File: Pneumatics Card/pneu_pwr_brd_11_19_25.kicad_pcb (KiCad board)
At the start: 4 copper layers, 59.9 x 60 mm, 62 parts, among them J1 2X1, J10 Conn_01x02, J11 Conn_01x02, J12 2X1, J2 2X1, J3 2X1, J4 2X1, J5 2X1, J6 2X1, J7 Conn_01x03_Pin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

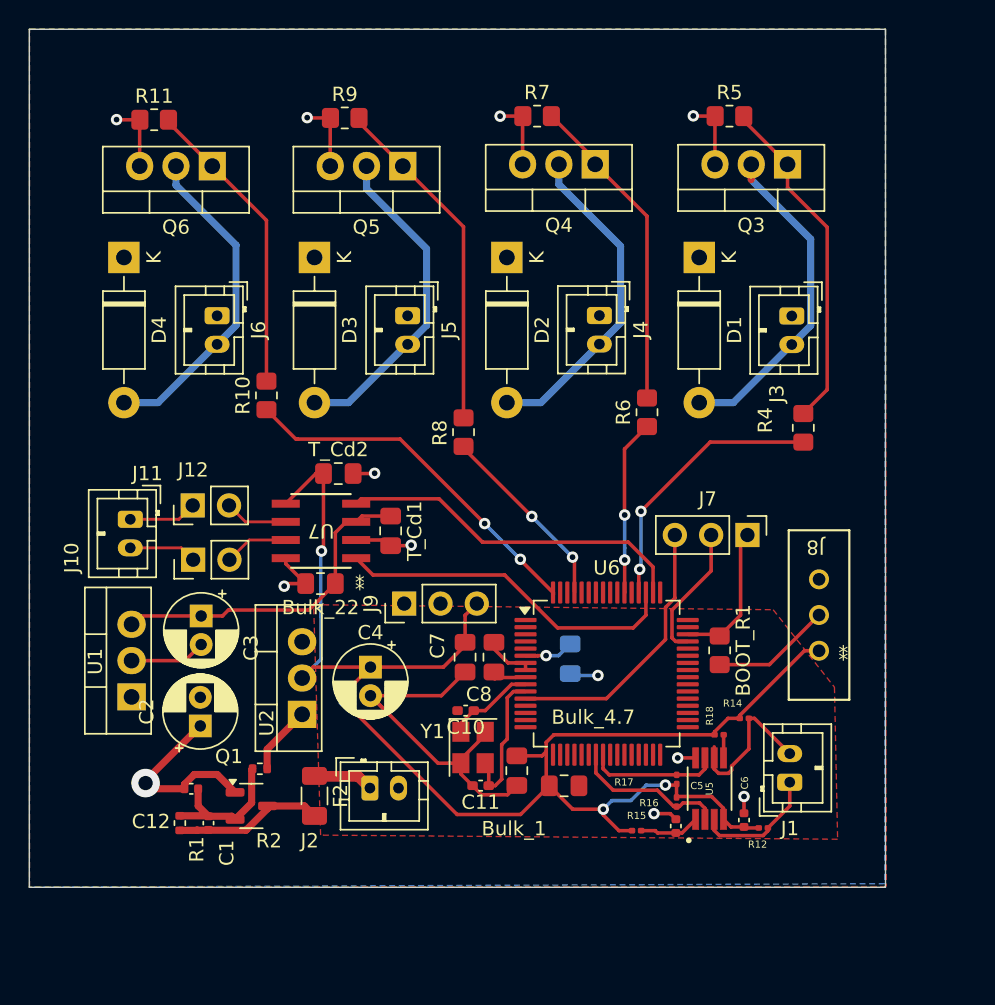
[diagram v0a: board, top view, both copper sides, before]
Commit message: Added the Mosfet drivers
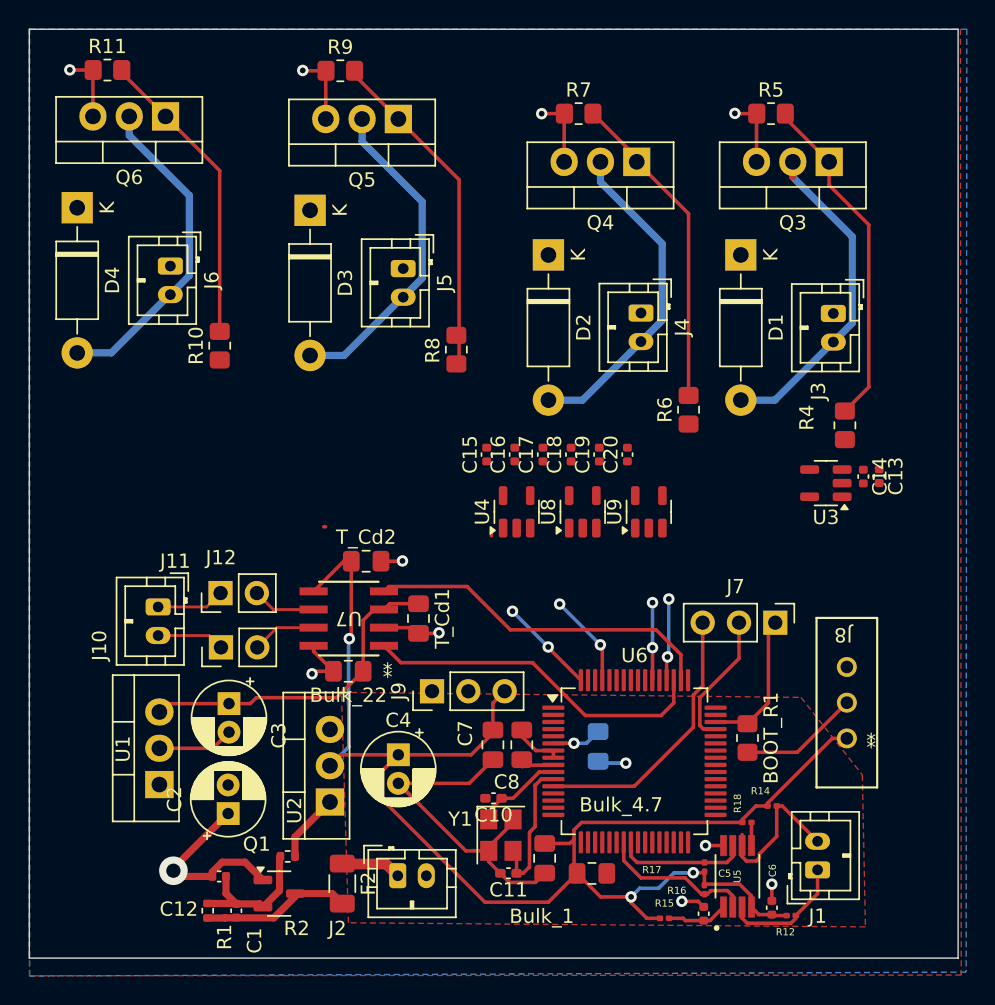
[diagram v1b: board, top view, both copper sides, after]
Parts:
- added C13: 1uF, Capacitor_SMD:C_0402_1005Metric, F.Cu at (204.8, 72.6)
- added C14: 0.1uF, Capacitor_SMD:C_0402_1005Metric, F.Cu at (203.7, 72.7)
- added C15: 0.1uF, Capacitor_SMD:C_0402_1005Metric, F.Cu at (177.3, 71.1)
- added C16: 1uF, Capacitor_SMD:C_0402_1005Metric, F.Cu at (179.3, 71.1)
- added C17: 0.1uF, Capacitor_SMD:C_0402_1005Metric, F.Cu at (181.2, 71.1)
- added C18: 1uF, Capacitor_SMD:C_0402_1005Metric, F.Cu at (183.2, 71.1)
- added C19: 0.1uF, Capacitor_SMD:C_0402_1005Metric, F.Cu at (185.2, 71.1)
- added C20: 1uF, Capacitor_SMD:C_0402_1005Metric, F.Cu at (187.1, 71.1)
- added U3: MCP1416, Package_TO_SOT_SMD:SOT-23-5, F.Cu at (201.0, 73.1)
- added U4: MCP1416, Package_TO_SOT_SMD:SOT-23-5, F.Cu at (179.4, 75.1)
- added U8: MCP1416, Package_TO_SOT_SMD:SOT-23-5, F.Cu at (184.0, 75.1)
- added U9: MCP1416, Package_TO_SOT_SMD:SOT-23-5, F.Cu at (188.6, 75.1)
- C1: value 4.7u -> 10nF
- Q1: value NTR0202PLT1G -> NTR0202PLT1G OR Si2347DS
- R1: value 47k -> 100k
- R2: value 100 -> 150k
- moved BOOT_R1 6.44 mm to (195.5, 91.0)
- moved Bulk_1 6.44 mm to (181.3, 99.4)
- moved Bulk_22 6.44 mm to (167.6, 86.3)
- moved Bulk_4.7 6.44 mm to (184.7, 100.4)
- moved C11 6.44 mm to (178.8, 100.4)
- moved C12 6.44 mm to (158.6, 100.6)
- moved C2 6.44 mm to (159.2, 96.2)
- moved C3 6.44 mm to (159.3, 88.5)
- moved C7 6.44 mm to (177.7, 91.4)
- moved C9 6.44 mm to (185.1, 91.5)
- moved F2 6.44 mm to (167.2, 101.1)
- moved J1 6.44 mm to (200.4, 100.2)
- moved J11 6.44 mm to (158.7, 80.8)
- moved J2 6.44 mm to (171.1, 100.6)
- moved J7 6.44 mm to (197.5, 82.9)
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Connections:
- R10 pad 1: S4CTRL -> Net-(U9-OUT)
- R4 pad 1: S1CTRL -> Net-(U3-OUT)
- R6 pad 1: S2CTRL -> Net-(U4-OUT)
- R8 pad 1: S3CTRL -> Net-(U8-OUT)
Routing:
- net S4CTRL: track 25.7 -> 7.24 mm
- net S1CTRL: track 19.3 -> 5.97 mm
- net S2CTRL: track 12.3 -> 5.45 mm
- net S3CTRL: track 13.4 -> 6.68 mm
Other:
- board size 59.9 x 60 mm -> 65 x 65 mm

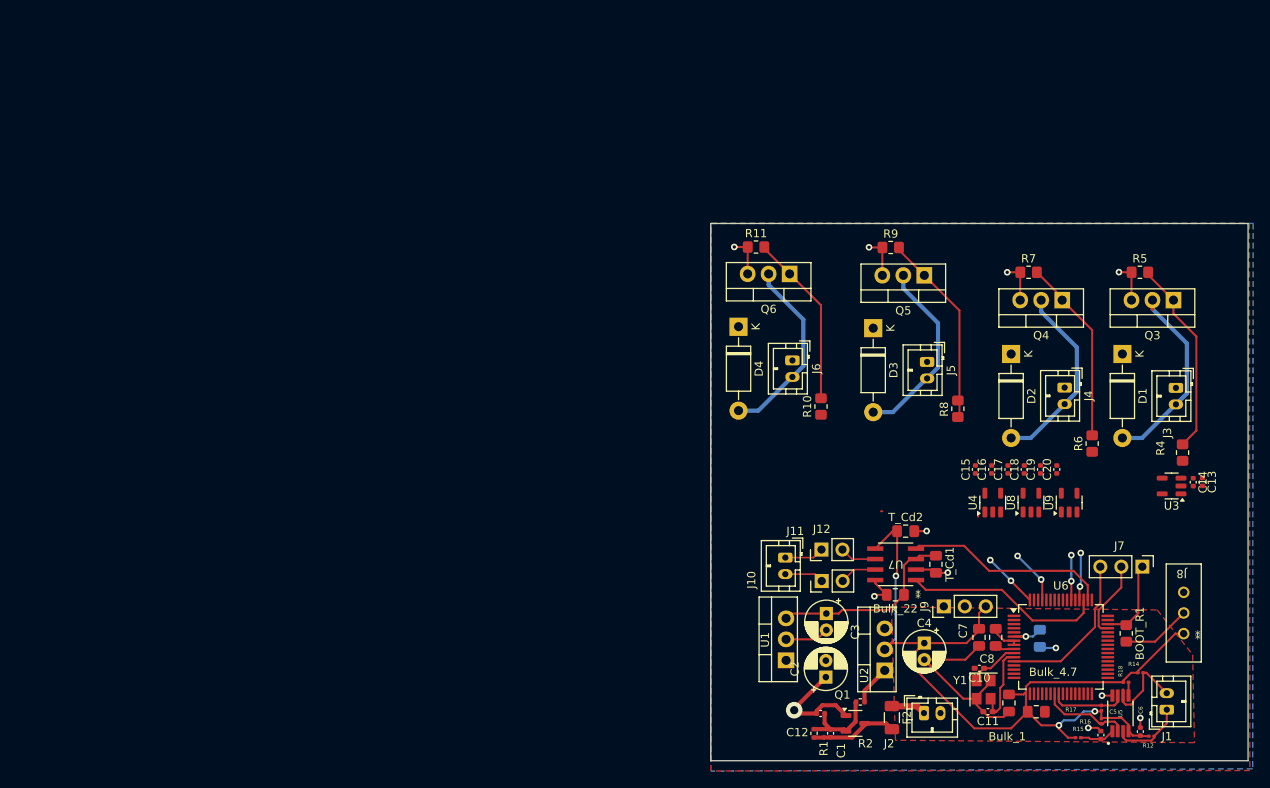
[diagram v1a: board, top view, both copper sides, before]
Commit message: Redid the Layout with new components
Increased board size to 63x63mm, added mounting holes (need to recheck), traces not routed yet.
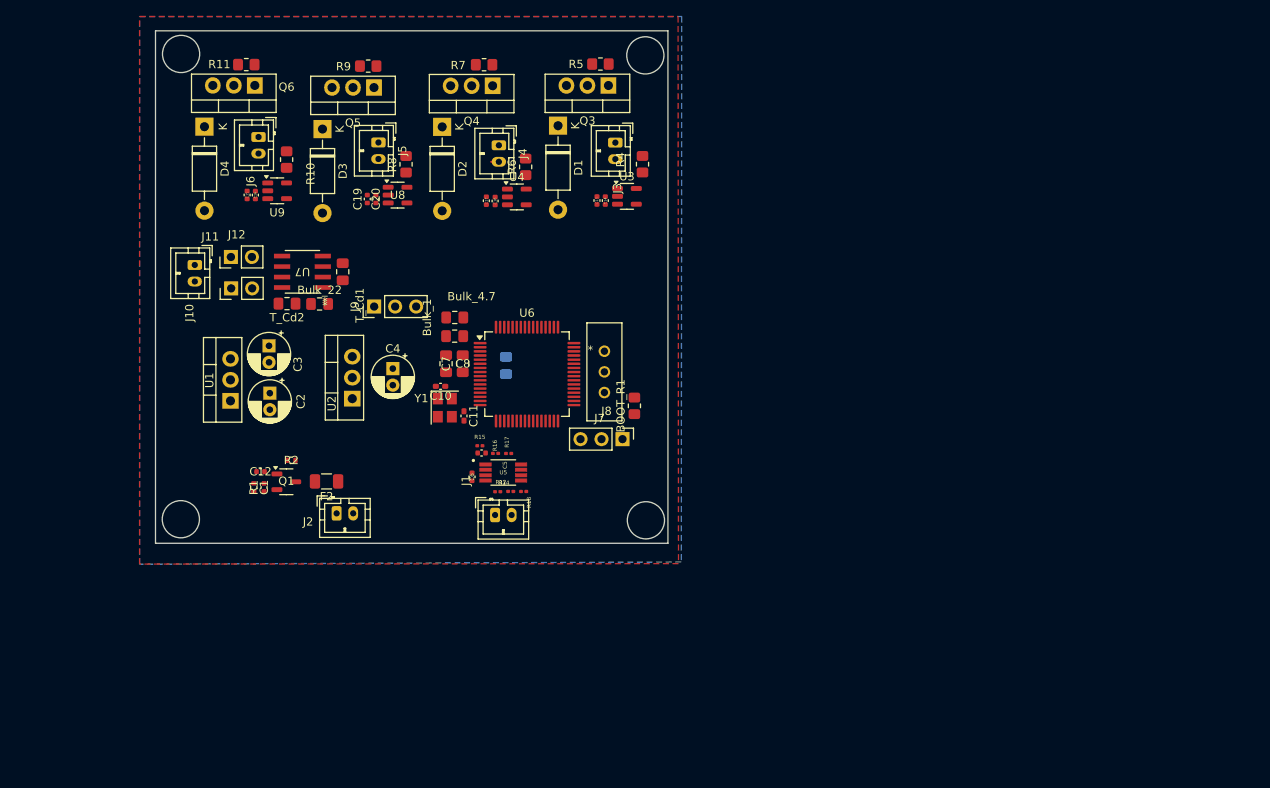
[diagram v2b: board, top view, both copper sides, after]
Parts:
- moved U9 103.0 mm to (92.8, 37.4), turned to 0 degrees
- moved C16 95.1 mm to (90.2, 37.9)
- moved C15 94.2 mm to (89.2, 37.9)
- moved C20 88.6 mm to (104.8, 38.4)
- moved C19 87.8 mm to (103.7, 38.4)
- moved C6 86.5 mm to (116.4, 72.0)
- moved U8 85.2 mm to (107.4, 37.9), turned to 0 degrees
- moved J1 84.6 mm to (119.2, 76.6), turned to 0 degrees
- moved R12 84.5 mm to (119.5, 73.8), turned to 0 degrees
- moved Bulk_4.7 83.8 mm to (114.3, 55.0)
- moved C5 82.3 mm to (117.6, 69.1), turned to 180 degrees
- moved Bulk_1 81.7 mm to (114.3, 52.7), turned to 180 degrees
- moved C13 80.8 mm to (131.5, 38.6), turned to 90 degrees
- moved R15 80.6 mm to (117.3, 68.2)
- moved U5 80.2 mm to (120.2, 71.5), turned to 0 degrees
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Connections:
- U6 pad 49: unconnected-(U6-PC9-Pad49) -> S1CTRL
- U6 pad 50: FDCAN_RX -> unconnected-(U6-PD0-Pad50)
- U6 pad 51: FDCAN_TX -> unconnected-(U6-PD1-Pad51)
- U6 pad 52: S1CTRL -> unconnected-(U6-PD2-Pad52)
- U6 pad 60: unconnected-(U6-PB6-Pad60) -> S3CTRL
- U6 pad 61: S3CTRL -> S4CTRL
- U6 pad 62: unconnected-(U6-PB8-Pad62) -> FDCAN_RX
- U6 pad 63: unconnected-(U6-PB9-Pad63) -> FDCAN_TX
- U6 pad 64: S4CTRL -> unconnected-(U6-PC10-Pad64)
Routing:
- net 3.3V: track 107.2 -> 0.00 mm, vias 3 -> 0
- net GND: track 74.0 -> 0.00 mm, vias 11 -> 0
- net FDCAN_RX: track 25.3 -> 0.00 mm
- net FDCAN_TX: track 24.3 -> 0.00 mm
- net Net-(Q5-G): track 24.0 -> 0.00 mm
- net Net-(Q3-G): track 23.9 -> 0.00 mm
- net 5V: track 23.4 -> 0.00 mm
- net SLN1-: track 23.0 -> 0.00 mm
- net SLN3-: track 23.0 -> 0.00 mm
- net SLN4-: track 23.0 -> 0.37 mm
- net Net-(Q4-G): track 22.5 -> 0.00 mm
- net SLN2-: track 23.2 -> 0.93 mm
- net Net-(Q6-G): track 21.1 -> 0.00 mm
- net /NRST: track 19.1 -> 0.00 mm
- net 12V: track 13.1 -> 0.00 mm, vias 1 -> 0
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- removed copper zone on F.Cu, net 3.3V
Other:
- board size 65 x 65 mm -> 62 x 62 mm

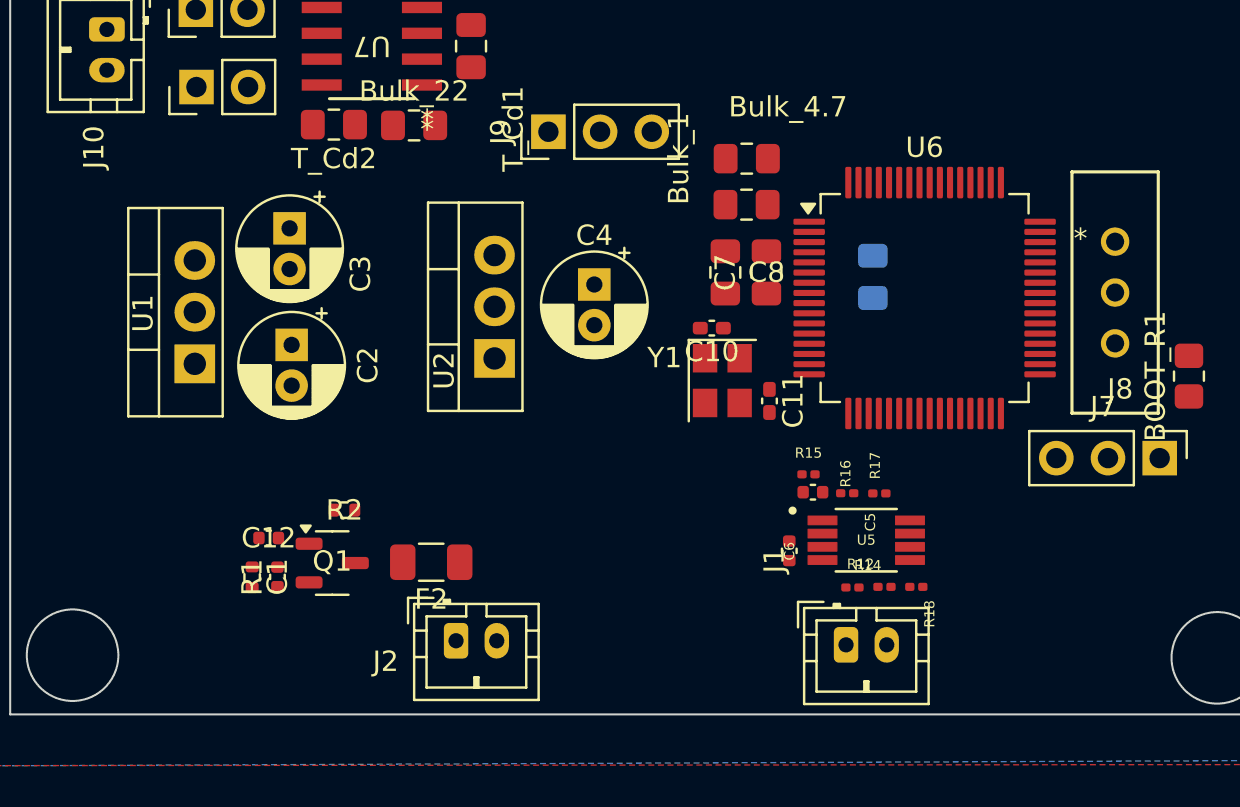
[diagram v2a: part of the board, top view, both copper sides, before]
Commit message: Moved the I2C protection for better tracing
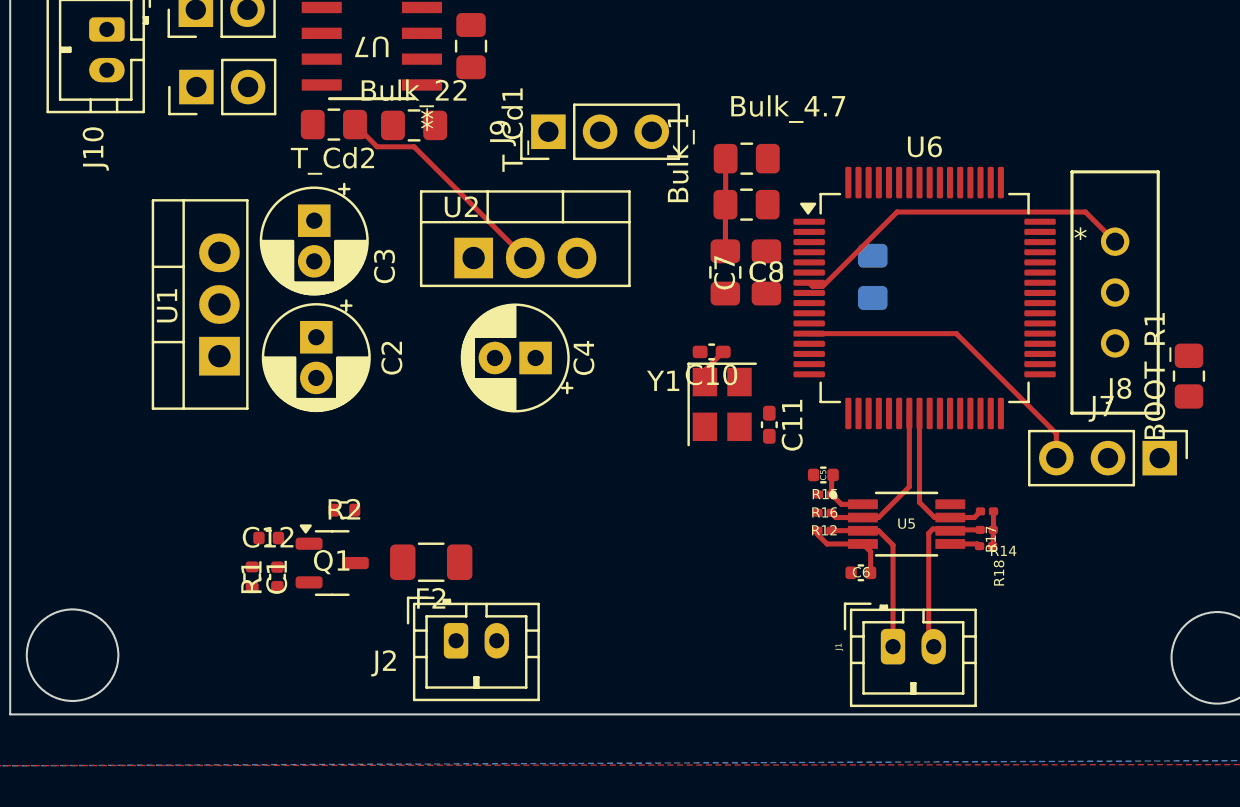
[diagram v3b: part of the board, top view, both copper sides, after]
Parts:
- moved R14 5.75 mm to (126.1, 71.0), turned to 180 degrees
- moved R17 5.37 mm to (126.1, 70.1), turned to 180 degrees
- moved U2 5.04 mm to (100.9, 57.6), turned to 0 degrees
- moved C4 4.62 mm to (103.9, 62.5), turned to 180 degrees
- moved R18 3.97 mm to (126.1, 71.8)
- moved C6 3.68 mm to (119.9, 73.1), turned to 0 degrees
- moved R12 3.11 mm to (118.1, 71.0), turned to 180 degrees
- moved J1 2.31 mm to (121.5, 76.7)
- moved U5 2.14 mm to (122.2, 70.7)
- moved R16 1.47 mm to (118.1, 70.1), turned to 180 degrees
- moved R15 1.28 mm to (118.2, 69.2)
- moved C2 1.27 mm to (93.1, 61.5)
- moved C3 1.27 mm to (93.0, 55.8)
- moved U1 1.27 mm to (88.4, 62.4)
- moved C11 1.17 mm to (115.4, 65.8)
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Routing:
- net 3.3V: track 0.00 -> 39.2 mm
- net /NRST: track 0.00 -> 15.4 mm
- net SDA_ext: track 0.00 -> 8.33 mm
- net SCL_ext: track 0.00 -> 8.31 mm
- net SDA: track 0.00 -> 8.17 mm
- net SCL: track 0.00 -> 7.80 mm
- net Net-(U5-EN): track 0.00 -> 2.73 mm
- net RCC_OSC_IN: track 0.00 -> 1.85 mm
- net Net-(U5-READY): track 0.00 -> 1.48 mm
